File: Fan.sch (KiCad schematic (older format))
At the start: 9 parts, among them Q2 MOSFET_N, Q3 MOSFET_N, Q4 MOSFET_N, U4 OPA4170, U5 MCP4922-E/P

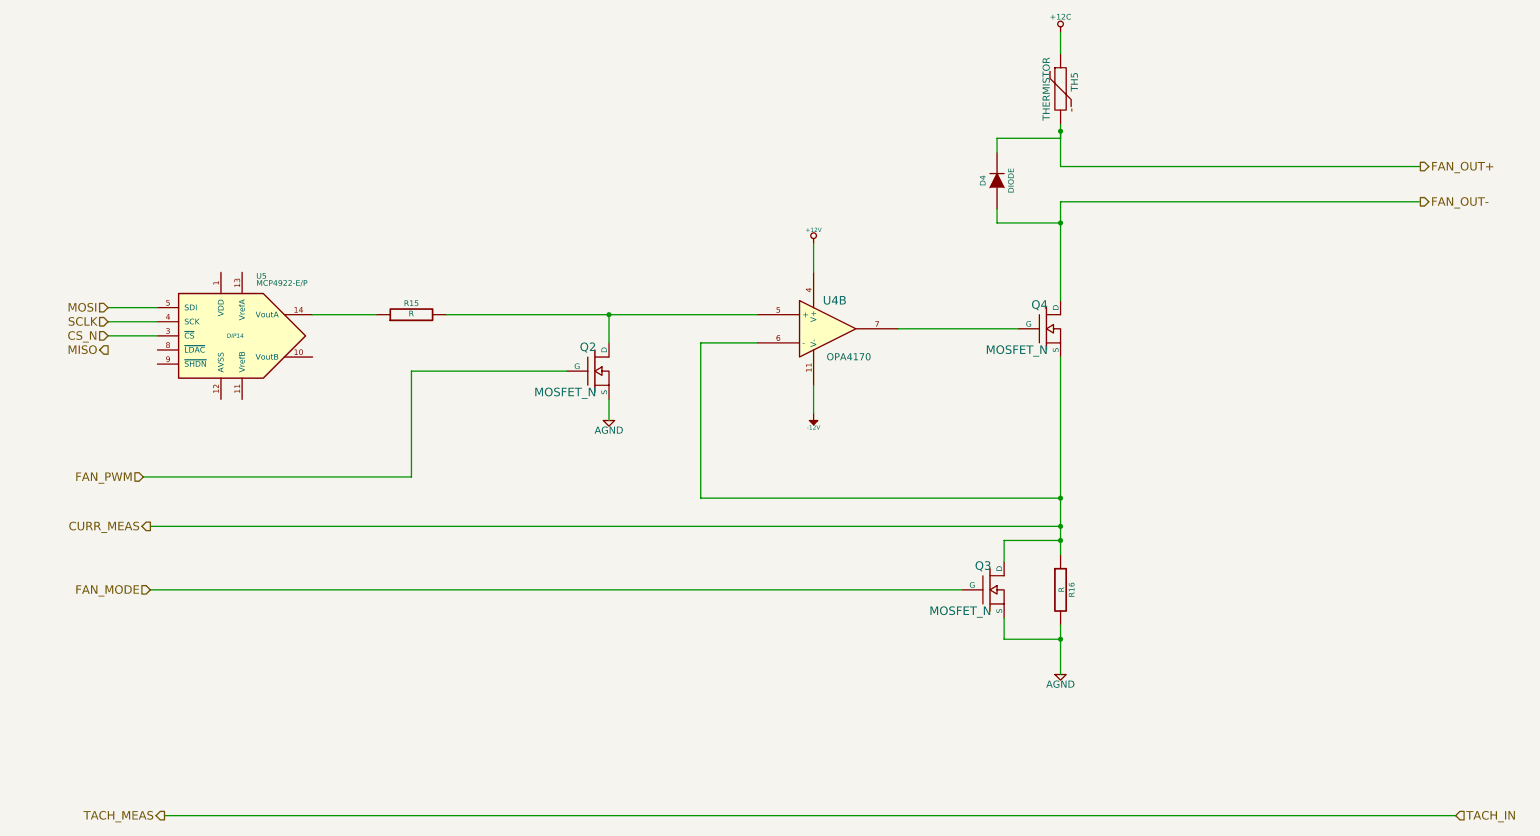
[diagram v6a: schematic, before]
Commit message: Associating Current Module
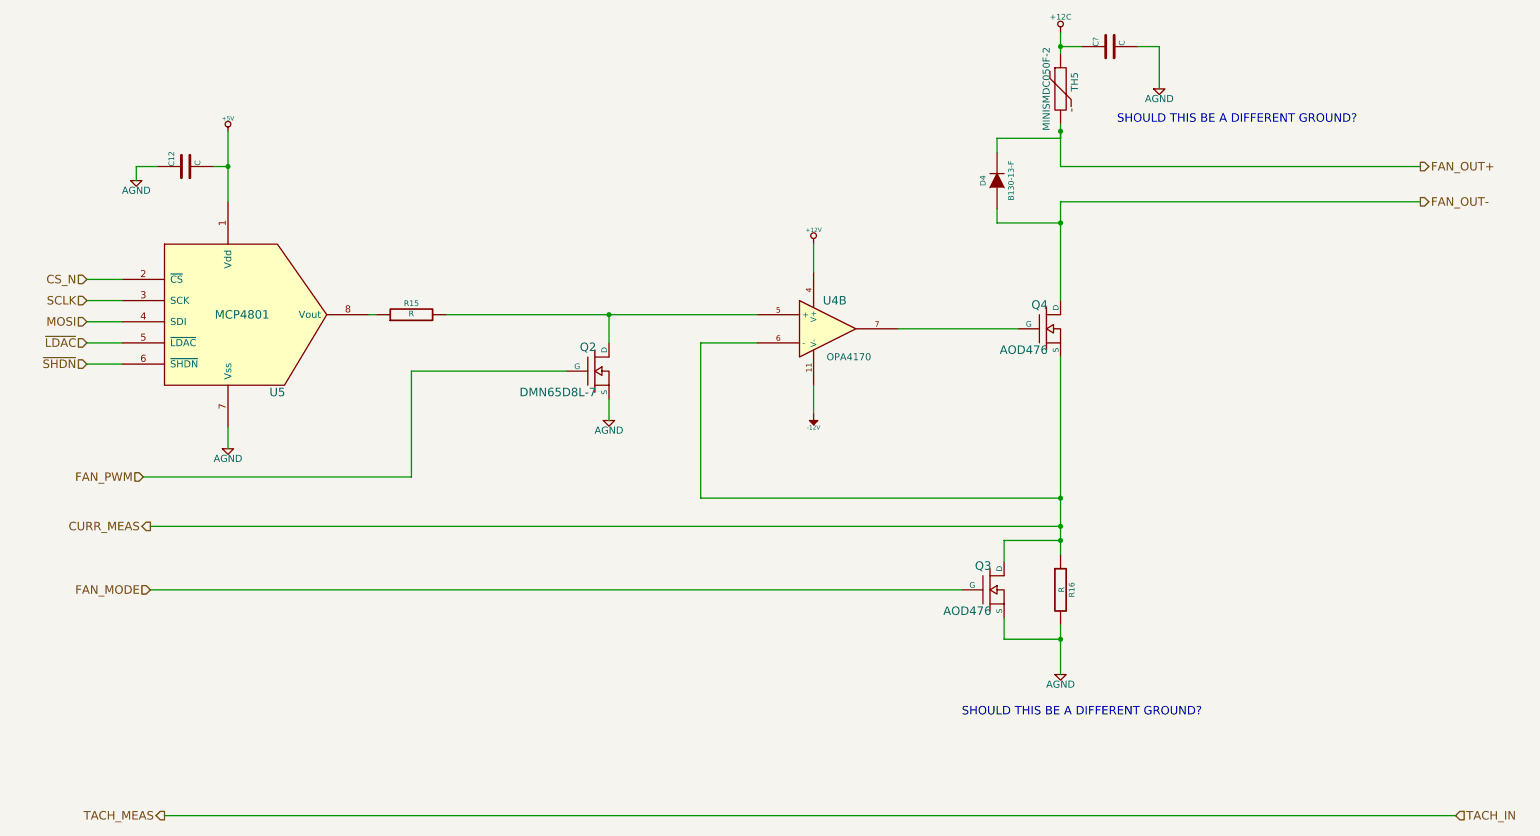
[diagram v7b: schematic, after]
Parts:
- removed U5: MCP4922-E/P, DIP14, symbol MCP4922-E/P
- added C12, C?: C, ~, symbol C
- added U5: MCP4801, symbol MCP4801
- D4: value DIODE -> B130-13-F; MFG Name (none) -> Diodes Inc; MFG Part Number (none) -> B130-13-F
- Q2: value MOSFET_N -> DMN65D8L-7; MFG Name (none) -> Diodes Inc; MFG Part Number (none) -> DMN65D8L-7
- Q3, Q4: value MOSFET_N -> AOD476; MFG Name (none) -> Alpha and Omega; MFG Part Number (none) -> AOD476
- TH5: value THERMISTOR -> MINISMDC050F-2; MFG Name (none) -> TE Connectivity; MFG Part Number (none) -> MINISMDC050F-2
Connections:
- net +12C: now also C?.1
- net AGND: now also C12.1, C?.2, U5.7 (Vss)
- net CS_N: now also U5.2 (~CS)
- net MOSI: now also U5.4 (SDI)
- net SCLK: now also U5.3 (SCK)
- net at R15.1: now also U5.8 (Vout)
- new net +5V: C12.2, U5.1 (Vdd)
- new net ~LDAC: U5.5 (~LDAC)
- new net ~SHDN: U5.6 (~SHDN)
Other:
- note added: "SHOULD THIS BE A DIFFERENT GROUND?"
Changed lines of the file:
@@
-EESchema Schematic File Version 2  date 10/13/2013 2:17:45 PM
+EESchema Schematic File Version 2  date 10/13/2013 8:19:10 PM
 LIBS:power
 LIBS:device
@@
 $Descr A4 11693 8268
 encoding utf-8
-Sheet 8 9
+Sheet 7 9
 Title ""
-Date "13 oct 2013"
+Date "14 oct 2013"
 Rev ""
 Comp ""
@@
 P 7800 3100
 F 0 "Q4" H 7810 3270 60  0000 R CNN
-F 1 "MOSFET_N" H 7810 2950 60  0000 R CNN
+F 1 "AOD476" H 7810 2950 60  0000 R CNN
 F 2 "~" H 7800 3100 60  0000 C CNN
 F 3 "~" H 7800 3100 60  0000 C CNN
+F 4 "Alpha and Omega" H 7800 3100 60  0001 C CNN "MFG Name"
+F 5 "AOD476" H 7800 3100 60  0001 C CNN "MFG Part Number"
 	1    7800 3100
 	1    0    0    -1
@@
 $EndComp
 $Comp
-L AGND #PWR60
+L AGND #PWR59
 U 1 1 523697F6
 P 7900 5550
-F 0 "#PWR60" H 7900 5550 40  0001 C CNN
+F 0 "#PWR59" H 7900 5550 40  0001 C CNN
 F 1 "AGND" H 7900 5480 50  0000 C CNN
 F 2 "" H 7900 5550 60  0000 C CNN
@@
 $EndComp
 $Comp
-L +12V #PWR57
+L +12V #PWR56
 U 1 1 5236981B
 P 6150 2500
-F 0 "#PWR57" H 6150 2450 20  0001 C CNN
+F 0 "#PWR56" H 6150 2450 20  0001 C CNN
 F 1 "+12V" H 6150 2600 30  0000 C CNN
 F 2 "" H 6150 2500 60  0000 C CNN
@@
 $EndComp
 $Comp
-L -12V #PWR58
+L -12V #PWR57
 U 1 1 5236982E
 P 6150 3700
-F 0 "#PWR58" H 6150 3830 20  0001 C CNN
+F 0 "#PWR57" H 6150 3830 20  0001 C CNN
 F 1 "-12V" H 6150 3800 30  0000 C CNN
 F 2 "" H 6150 3700 60  0000 C CNN
@@
 $EndComp
 $Comp
-L AGND #PWR56
+L AGND #PWR55
 U 1 1 523698EE
 P 4700 3750
-F 0 "#PWR56" H 4700 3750 40  0001 C CNN
+F 0 "#PWR55" H 4700 3750 40  0001 C CNN
 F 1 "AGND" H 4700 3680 50  0000 C CNN
 F 2 "" H 4700 3750 60  0000 C CNN
 F 3 "" H 4700 3750 60  0000 C CNN
 	1    4700 3750
-	1    0    0    -1
-$EndComp
-$Comp
-L MCP4922-E/P U5
-U 1 1 52369914
-P 2050 3150
-F 0 "U5" H 2200 3550 40  0000 L BNN
-F 1 "MCP4922-E/P" H 2200 3500 40  0000 L BNN
-F 2 "DIP14" H 2050 3150 30  0000 C CIN
-F 3 "" H 2050 3150 60  0000 C CNN
-	1    2050 3150
 	1    0    0    -1
 $EndComp
@@
 	0    -1   -1   0
 $EndComp
-Text HLabel 1150 2950 0    60   Input ~ 0
+Text HLabel 1000 3050 0    60   Input ~ 0
 MOSI
-Text HLabel 1150 3250 0    60   Output ~ 0
-MISO
-Text HLabel 1150 3150 0    60   Input ~ 0
+Text HLabel 1000 2750 0    60   Input ~ 0
 CS_N
-Text HLabel 1150 3050 0    60   Input ~ 0
+Text HLabel 1000 2900 0    60   Input ~ 0
 SCLK
 $Comp
@@
 P 7400 4950
 F 0 "Q3" H 7410 5120 60  0000 R CNN
-F 1 "MOSFET_N" H 7410 4800 60  0000 R CNN
+F 1 "AOD476" H 7410 4800 60  0000 R CNN
 F 2 "~" H 7400 4950 60  0000 C CNN
 F 3 "~" H 7400 4950 60  0000 C CNN
+F 4 "Alpha and Omega" H 7400 4950 60  0001 C CNN "MFG Name"
+F 5 "AOD476" H 7400 4950 60  0001 C CNN "MFG Part Number"
 	1    7400 4950
 	1    0    0    -1
@@
 P 7900 1400
 F 0 "TH5" V 8000 1450 50  0000 C CNN
-F 1 "THERMISTOR" V 7800 1400 50  0000 C CNN
+F 1 "MINISMDC050F-2" V 7800 1400 50  0000 C CNN
 F 2 "~" H 7900 1400 60  0000 C CNN
 F 3 "~" H 7900 1400 60  0000 C CNN
+F 4 "TE Connectivity" H 7900 1400 60  0001 C CNN "MFG Name"
+F 5 "MINISMDC050F-2" H 7900 1400 60  0001 C CNN "MFG Part Number"
 	1    7900 1400
 	1    0    0    -1
@@
 P 7450 2050
 F 0 "D4" H 7450 2150 40  0000 C CNN
-F 1 "DIODE" H 7450 1950 40  0000 C CNN
+F 1 "B130-13-F" H 7450 1950 40  0000 C CNN
 F 2 "~" H 7450 2050 60  0000 C CNN
 F 3 "~" H 7450 2050 60  0000 C CNN
+F 4 "Diodes Inc" H 7450 2050 60  0001 C CNN "MFG Name"
+F 5 "B130-13-F" H 7450 2050 60  0001 C CNN "MFG Part Number"
 	1    7450 2050
 	0    -1   -1   0
@@
 P 4600 3400
 F 0 "Q2" H 4610 3570 60  0000 R CNN
-F 1 "MOSFET_N" H 4610 3250 60  0000 R CNN
+F 1 "DMN65D8L-7" H 4610 3250 60  0000 R CNN
 F 2 "~" H 4600 3400 60  0000 C CNN
 F 3 "~" H 4600 3400 60  0000 C CNN
+F 4 "Diodes Inc" H 4600 3400 60  0001 C CNN "MFG Name"
+F 5 "DMN65D8L-7" H 4600 3400 60  0001 C CNN "MFG Part Number"
 	1    4600 3400
 	1    0    0    -1
@@
 	1400 4150 3300 4150
 Wire Wire Line
-	2600 3000 3050 3000
-Wire Wire Line
-	1150 2950 1500 2950
-Wire Wire Line
-	1150 3050 1500 3050
-Wire Wire Line
-	1150 3150 1500 3150
+	3000 3000 3050 3000
 Wire Wire Line
 	7900 1000 7900 1150
@@
 FAN_MODE
 $Comp
-L +12C #PWR59
+L +12C #PWR58
 U 1 1 5243907A
 P 7900 1000
-F 0 "#PWR59" H 7900 970 30  0001 C CNN
+F 0 "#PWR58" H 7900 970 30  0001 C CNN
 F 1 "+12C" H 7900 1110 40  0000 C CNN
 F 2 "~" H 7900 1000 60  0000 C CNN
@@
 	1    0    0    -1
 $EndComp
+$Comp
+L MCP4801 U5
+U 1 1 525B0EF5
+P 2000 2750
+F 0 "U5" H 2350 1950 60  0000 C CNN
+F 1 "MCP4801" H 2100 2500 60  0000 C CNN
+F 2 "" H 2000 2750 60  0000 C CNN
+F 3 "" H 2000 2750 60  0000 C CNN
+	1    2000 2750
+	1    0    0    -1
+$EndComp
+Wire Wire Line
+	1250 2750 1000 2750
+Wire Wire Line
+	1250 2900 1000 2900
+Wire Wire Line
+	1250 3050 1000 3050
+Text HLabel 1000 3200 0    60   Input ~ 0
+~LDAC
+Wire Wire Line
+	1000 3200 1250 3200
+Text HLabel 1000 3350 0    60   Input ~ 0
+~SHDN
+Wire Wire Line
+	1000 3350 1250 3350
+$Comp
+L C C12
+U 1 1 525C14EF
+P 1700 1950
+F 0 "C12" H 1700 2050 40  0000 L CNN
+F 1 "C" H 1706 1865 40  0000 L CNN
+F 2 "~" H 1738 1800 30  0000 C CNN
+F 3 "~" H 1700 1950 60  0000 C CNN
+	1    1700 1950
+	0    -1   -1   0
+$EndComp
+Wire Wire Line
+	2000 1700 2000 2200
+Wire Wire Line
+	2000 1950 1900 1950
+Connection ~ 2000 1950
+$Comp
+L AGND #PWR52
+U 1 1 525C14F8
+P 1350 2050
+F 0 "#PWR52" H 1350 2050 40  0001 C CNN
+F 1 "AGND" H 1350 1980 50  0000 C CNN
+F 2 "" H 1350 2050 60  0000 C CNN
+F 3 "" H 1350 2050 60  0000 C CNN
+	1    1350 2050
+	1    0    0    -1
+$EndComp
+Wire Wire Line
+	1350 2050 1350 1950
+Wire Wire Line
+	1350 1950 1500 1950
+$Comp
+L +5V #PWR53
+U 1 1 525C1500
+P 2000 1700
+F 0 "#PWR53" H 2000 1790 20  0001 C CNN
+F 1 "+5V" H 2000 1790 30  0000 C CNN
+F 2 "~" H 2000 1700 60  0000 C CNN
+F 3 "~" H 2000 1700 60  0000 C CNN
+	1    2000 1700
+	1    0    0    -1
+$EndComp
+$Comp
+L AGND #PWR54
+U 1 1 525C1506
+P 2000 3950
+F 0 "#PWR54" H 2000 3950 40  0001 C CNN
+F 1 "AGND" H 2000 3880 50  0000 C CNN
+F 2 "" H 2000 3950 60  0000 C CNN
+F 3 "" H 2000 3950 60  0000 C CNN
+	1    2000 3950
+	1    0    0    -1
+$EndComp
+Wire Wire Line
+	2000 3950 2000 3800
+$Comp
+L C C?
+U 1 1 525C19B8
+P 8250 1100
+F 0 "C?" H 8250 1200 40  0000 L CNN
+F 1 "C" H 8256 1015 40  0000 L CNN
+F 2 "~" H 8288 950 30  0000 C CNN
+F 3 "~" H 8250 1100 60  0000 C CNN
+	1    8250 1100
+	0    -1   -1   0
+$EndComp
+Wire Wire Line
+	8050 1100 7900 1100
+Connection ~ 7900 1100
+Wire Wire Line
+	8450 1100 8600 1100
+Wire Wire Line
+	8600 1100 8600 1400
+$Comp
+L AGND #PWR?
+U 1 1 525C1A28
+P 8600 1400
+F 0 "#PWR?" H 8600 1400 40  0001 C CNN
+F 1 "AGND" H 8600 1330 50  0000 C CNN
+F 2 "" H 8600 1400 60  0000 C CNN
+F 3 "" H 8600 1400 60  0000 C CNN
+	1    8600 1400
+	1    0    0    -1
+$EndComp
+Text Notes 8300 1650 0    60   ~ 0
+SHOULD THIS BE A DIFFERENT GROUND?
+Text Notes 7200 5850 0    60   ~ 0
+SHOULD THIS BE A DIFFERENT GROUND?
 $EndSCHEMATC

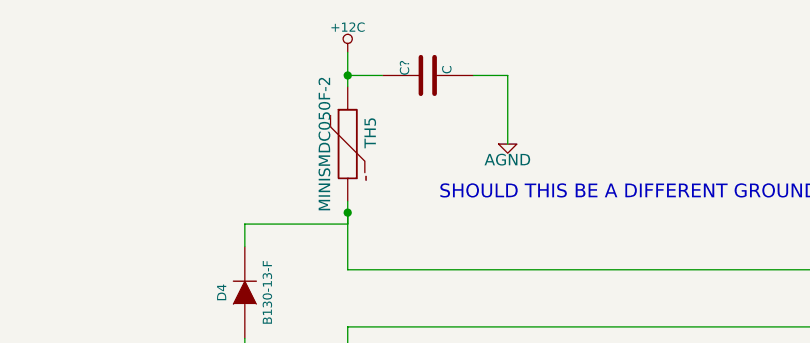
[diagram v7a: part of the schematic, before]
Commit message: Placing Current Module Components
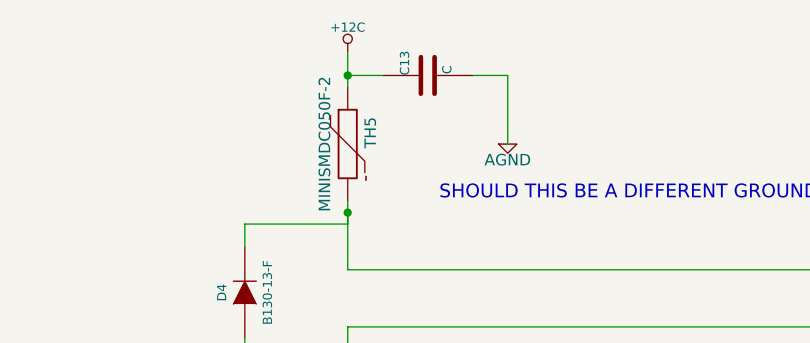
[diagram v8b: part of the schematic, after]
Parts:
- removed Q3, Q4: AOD476, ~, symbol MOSFET_N
- added Q3, Q4: AOD476, ~, symbol MOS_N_NUM
- gave numbers to parts that had none: 1
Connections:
- net AGND: now also Q3.3 (S)
- net CURR_MEAS: now also Q3.2 (D), Q4.3 (S)
- net FAN_MODE: now also Q3.1 (G)
- net FAN_OUT-: now also Q4.2 (D)
- net at U4.7: now also Q4.1 (G)
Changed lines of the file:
@@
-EESchema Schematic File Version 2  date 10/13/2013 8:19:10 PM
+EESchema Schematic File Version 2  date 10/13/2013 8:46:30 PM
 LIBS:power
 LIBS:device
@@
 $EndComp
 $Comp
-L MOSFET_N Q4
-U 1 1 523697B6
-P 7800 3100
-F 0 "Q4" H 7810 3270 60  0000 R CNN
-F 1 "AOD476" H 7810 2950 60  0000 R CNN
-F 2 "~" H 7800 3100 60  0000 C CNN
-F 3 "~" H 7800 3100 60  0000 C CNN
-F 4 "Alpha and Omega" H 7800 3100 60  0001 C CNN "MFG Name"
-F 5 "AOD476" H 7800 3100 60  0001 C CNN "MFG Part Number"
-	1    7800 3100
-	1    0    0    -1
-$EndComp
-$Comp
 L R R16
 U 1 1 523697E7
@@
 Text HLabel 1000 2900 0    60   Input ~ 0
 SCLK
-$Comp
-L MOSFET_N Q3
-U 1 1 5243896F
-P 7400 4950
-F 0 "Q3" H 7410 5120 60  0000 R CNN
-F 1 "AOD476" H 7410 4800 60  0000 R CNN
-F 2 "~" H 7400 4950 60  0000 C CNN
-F 3 "~" H 7400 4950 60  0000 C CNN
-F 4 "Alpha and Omega" H 7400 4950 60  0001 C CNN "MFG Name"
-F 5 "AOD476" H 7400 4950 60  0001 C CNN "MFG Part Number"
-	1    7400 4950
-	1    0    0    -1
-$EndComp
 $Comp
 L THERMISTOR TH5
@@
 	2000 3950 2000 3800
 $Comp
-L C C?
+L C C13
 U 1 1 525C19B8
 P 8250 1100
-F 0 "C?" H 8250 1200 40  0000 L CNN
+F 0 "C13" H 8250 1200 40  0000 L CNN
 F 1 "C" H 8256 1015 40  0000 L CNN
 F 2 "~" H 8288 950 30  0000 C CNN
@@
 	8600 1100 8600 1400
 $Comp
-L AGND #PWR?
+L AGND #PWR60
 U 1 1 525C1A28
 P 8600 1400
-F 0 "#PWR?" H 8600 1400 40  0001 C CNN
+F 0 "#PWR60" H 8600 1400 40  0001 C CNN
 F 1 "AGND" H 8600 1330 50  0000 C CNN
 F 2 "" H 8600 1400 60  0000 C CNN
@@
 Text Notes 7200 5850 0    60   ~ 0
 SHOULD THIS BE A DIFFERENT GROUND?
+$Comp
+L MOS_N_NUM Q4
+U 1 1 525B42A5
+P 7800 3100
+F 0 "Q4" H 7810 3270 60  0000 R CNN
+F 1 "AOD476" H 7810 2950 60  0000 R CNN
+F 2 "~" H 7800 3100 60  0000 C CNN
+F 3 "~" H 7800 3100 60  0000 C CNN
+F 4 "Alpha and Omega" H 7800 3100 60  0001 C CNN "MFG Name"
+F 5 "AOD476" H 7800 3100 60  0001 C CNN "MFG Part Number"
+	1    7800 3100
+	1    0    0    -1
+$EndComp
+$Comp
+L MOS_N_NUM Q3
+U 1 1 525B433B
+P 7400 4950
+F 0 "Q3" H 7410 5120 60  0000 R CNN
+F 1 "AOD476" H 7410 4800 60  0000 R CNN
+F 2 "~" H 7400 4950 60  0000 C CNN
+F 3 "~" H 7400 4950 60  0000 C CNN
+F 4 "Alpha and Omega" H 7400 4950 60  0001 C CNN "MFG Name"
+F 5 "AOD476" H 7400 4950 60  0001 C CNN "MFG Part Number"
+	1    7400 4950
+	1    0    0    -1
+$EndComp
 $EndSCHEMATC
